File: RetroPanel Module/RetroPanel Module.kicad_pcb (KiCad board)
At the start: 2 copper layers, 100 x 97.9 mm, 77 parts, among them J1 Front Panel, J10 SW_EXTRA, J11 RS-232, J12 +5VSB, J13 PWR_ON, J14 PWR_OK, J15 COMMON, J16 SPEAKER, J17 LED_HDD, J2 SW_POWER, J3 LED_POWER, J4 SW_RESET, J5 SW_TURBO, J6 LED_TURBO, J7 POWER, J8 IIC, J9 POST_CARD, M1 Mounting_Pin, M10 Mounting_Pad, M11 Mounting_Pad, M12 Mounting_Pad, M13 Mounting_Pad, M14 Mounting_Pad, M15 Mounting_Pad, M16 Mounting_Pin, M2 Mounting_Pin, M3 Mounting_Pin, M4 Mounting_Pad, M5 Mounting_Pad, M6 Mounting_Pad, M7 Mounting_Pad, M8 Mounting_Pad, M9 Mounting_Pad, Q1 2N3904, Q2 2N3904, Q3 2N3904, Q4 2N3904, U1 MAX232, U2 NE555P

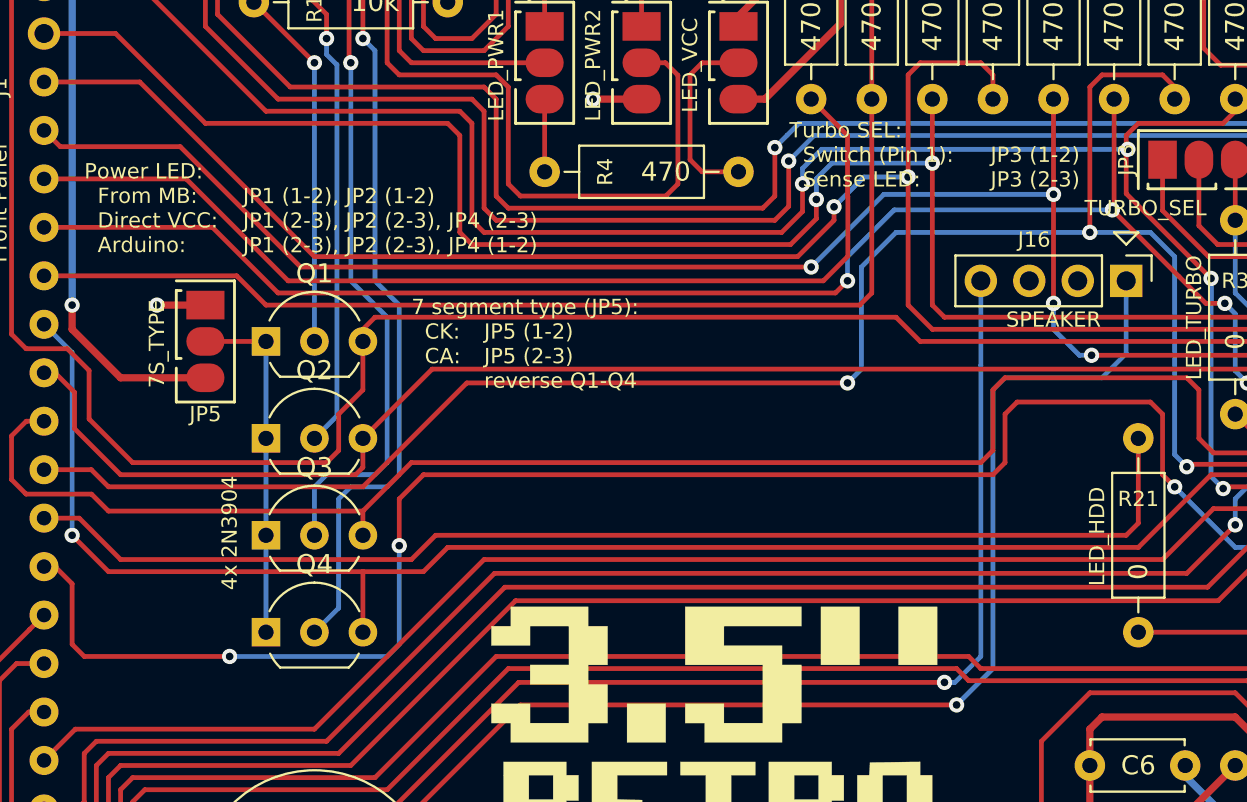
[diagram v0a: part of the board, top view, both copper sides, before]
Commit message: Better description for CA display usage
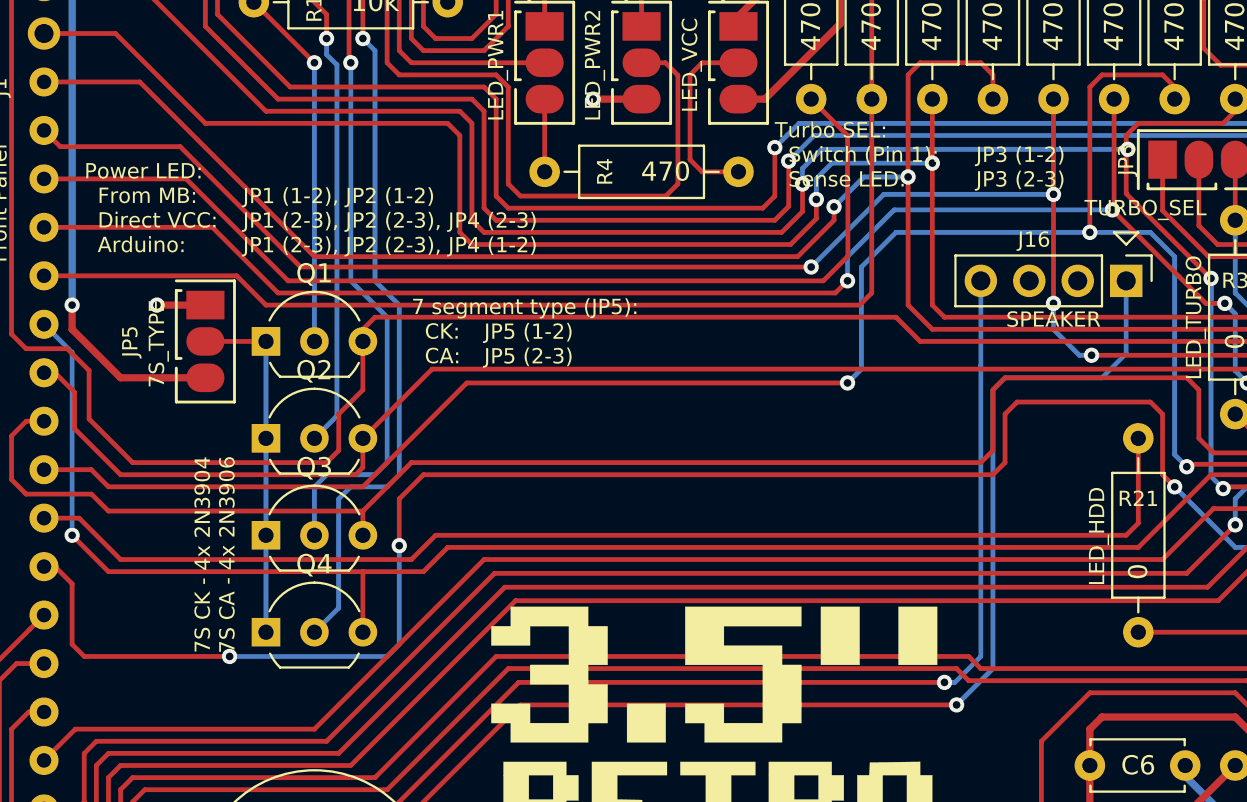
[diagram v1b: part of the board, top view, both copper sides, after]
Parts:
- Q1, Q2, Q3, Q4: value 2N3904 -> 2N3904/2N3906
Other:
- board text added: "7S CK - 4x 2N3904 7S CA - 4x 2N3906"
- board text added: "JP5 (1-2) JP5 (2-3)"
- board text removed: "4x 2N3904"
- board text removed: "JP5 (1-2) JP5 (2-3) reverse Q1-Q4"

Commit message: Tweaked resistor value to work better 7S CA
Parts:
- Q1, Q2, Q3, Q4: value 2N3904/2N3906 -> 2N3904 *
- R13, R14, R15, R16: value 10k -> 3k3
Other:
- board text added: "4x 2N3904 4x 2N3906 (install backwards)"
- board text added: "7 segment type (JP5): 7S CK: 7S CA:"
- board text added: "Q1-Q4: 7S CK: 7S CA:"
- board text removed: "7 segment type (JP5): CK: CA:"
- board text removed: "7S CK - 4x 2N3904 7S CA - 4x 2N3906"
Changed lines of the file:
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@@
   (general
     (thickness 1.6)
-    (drawings 86)
+    (drawings 87)
     (tracks 959)
     (zones 0)
@@
       (effects (font (size 0.8 0.8) (thickness 0.1)))
     )
-    (fp_text value 10k (at 3.81 0) (layer F.SilkS)
+    (fp_text value 3k3 (at 3.81 0) (layer F.SilkS)
       (effects (font (size 1 1) (thickness 0.15)))
     )
@@
       (effects (font (size 0.8 0.8) (thickness 0.1)))
     )
-    (fp_text value 10k (at 3.81 0) (layer F.SilkS)
+    (fp_text value 3k3 (at 3.81 0) (layer F.SilkS)
       (effects (font (size 1 1) (thickness 0.15)))
     )
@@
       (effects (font (size 0.8 0.8) (thickness 0.1)))
     )
-    (fp_text value 10k (at 3.81 0) (layer F.SilkS)
+    (fp_text value 3k3 (at 3.81 0) (layer F.SilkS)
       (effects (font (size 1 1) (thickness 0.15)))
     )
@@
       (effects (font (size 0.8 0.8) (thickness 0.1)))
     )
-    (fp_text value 10k (at 3.81 0) (layer F.SilkS)
+    (fp_text value 3k3 (at 3.81 0) (layer F.SilkS)
       (effects (font (size 1 1) (thickness 0.15)))
     )
@@
       (effects (font (size 1 1) (thickness 0.15)))
     )
-    (fp_text value 2N3904/2N3906 (at 2.54 2.79) (layer F.Fab)
+    (fp_text value "2N3904 *" (at 2.54 2.79) (layer F.Fab)
       (effects (font (size 1 1) (thickness 0.15)))
     )
@@
     (descr "TO-92 leads in-line, wide, drill 0.75mm (see NXP sot054_po.pdf)")
     (tags "to-92 sc-43 sc-43a sot54 PA33 transistor")
-    (fp_text reference Q2 (at 2.54 -3.56) (layer F.SilkS)
+    (fp_text reference Q2 (at -1.905 0 90) (layer F.SilkS)
       (effects (font (size 1 1) (thickness 0.15)))
     )
-    (fp_text value 2N3904/2N3906 (at 2.54 2.79) (layer F.Fab)
+    (fp_text value "2N3904 *" (at 2.54 2.79) (layer F.Fab)
       (effects (font (size 1 1) (thickness 0.15)))
     )
@@
     (descr "TO-92 leads in-line, wide, drill 0.75mm (see NXP sot054_po.pdf)")
     (tags "to-92 sc-43 sc-43a sot54 PA33 transistor")
-    (fp_text reference Q3 (at 2.54 -3.56) (layer F.SilkS)
+    (fp_text reference Q3 (at -1.905 0 90) (layer F.SilkS)
       (effects (font (size 1 1) (thickness 0.15)))
     )
-    (fp_text value 2N3904/2N3906 (at 2.54 2.79) (layer F.Fab)
+    (fp_text value "2N3904 *" (at 2.54 2.79) (layer F.Fab)
       (effects (font (size 1 1) (thickness 0.15)))
     )
@@
     (descr "TO-92 leads in-line, wide, drill 0.75mm (see NXP sot054_po.pdf)")
     (tags "to-92 sc-43 sc-43a sot54 PA33 transistor")
-    (fp_text reference Q4 (at 2.54 -3.56) (layer F.SilkS)
+    (fp_text reference Q4 (at -1.905 0 90) (layer F.SilkS)
       (effects (font (size 1 1) (thickness 0.15)))
     )
-    (fp_text value 2N3904/2N3906 (at 2.54 2.79) (layer F.Fab)
+    (fp_text value "2N3904 *" (at 2.54 2.79) (layer F.Fab)
       (effects (font (size 1 1) (thickness 0.15)))
     )
@@
     )
   )
+  (gr_text "\n4x 2N3904\n4x 2N3906 (install backwards)" (at 142.487 112.689) (layer F.SilkS)
+    (effects (font (size 0.8 0.8) (thickness 0.1)) (justify left))
+  )
   (gr_text LED_TURBO (at 177.666 110.276 90) (layer F.SilkS)
     (effects (font (size 0.8 0.8) (thickness 0.1)) (justify left))
@@
     (effects (font (size 0.8 0.8) (thickness 0.1)) (justify left))
   )
-  (gr_text "7S CK - 4x 2N3904\n7S CA - 4x 2N3906" (at 126.358 119.42 90) (layer F.SilkS)
-    (effects (font (size 0.8 0.8) (thickness 0.1)))
+  (gr_text "Q1-Q4:\n  7S CK:\n  7S CA:" (at 136.645 112.689) (layer F.SilkS)
+    (effects (font (size 0.8 0.8) (thickness 0.1)) (justify left))
   )
-  (gr_text "\nJP5 (1-2)\nJP5 (2-3)" (at 140.455 107.736) (layer F.SilkS)
+  (gr_text "\nJP5 (1-2)\nJP5 (2-3)" (at 142.487 107.736) (layer F.SilkS)
     (effects (font (size 0.8 0.8) (thickness 0.1)) (justify left))
   )
-  (gr_text "7 segment type (JP5):\n  CK:\n  CA:\n\n" (at 136.645 108.371) (layer F.SilkS)
+  (gr_text "7 segment type (JP5):\n  7S CK:\n  7S CA:\n\n" (at 136.645 108.371) (layer F.SilkS)
     (effects (font (size 0.8 0.8) (thickness 0.1)) (justify left))
   )

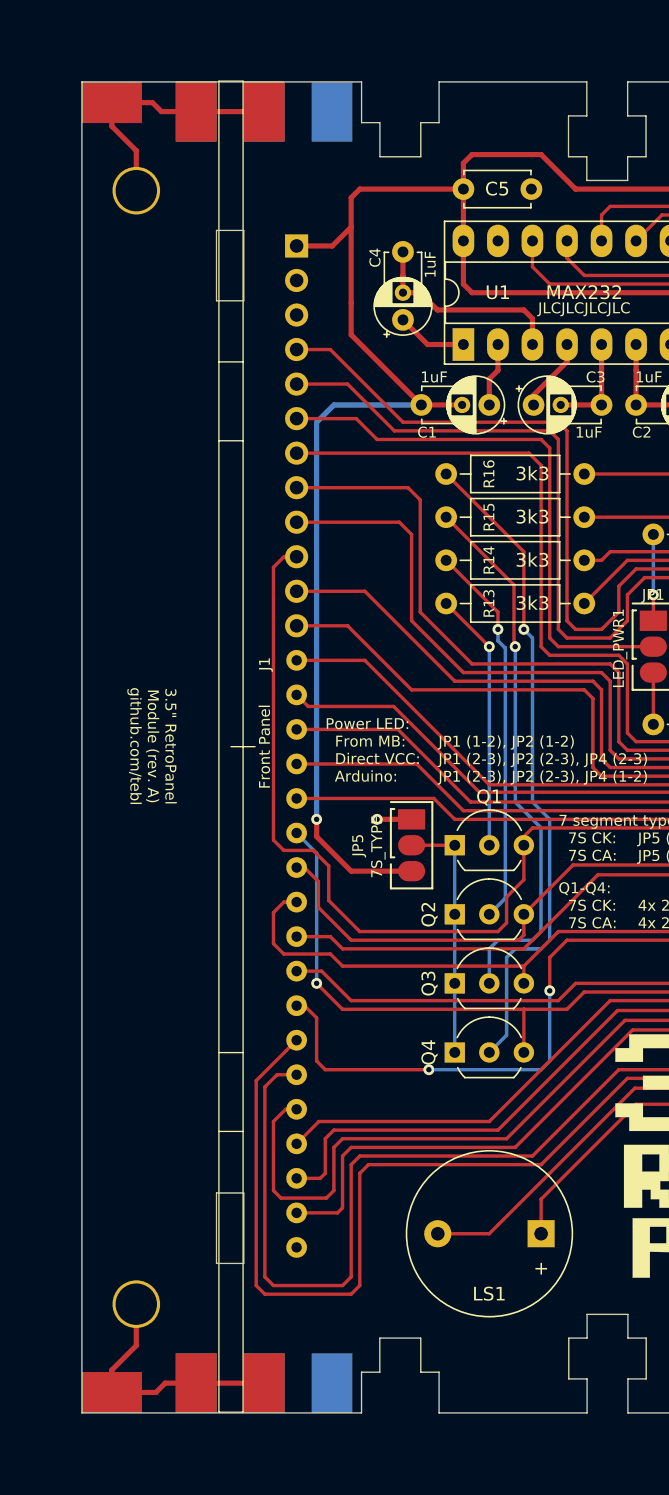
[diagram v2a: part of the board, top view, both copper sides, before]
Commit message: Adjustable mounting with huge pads
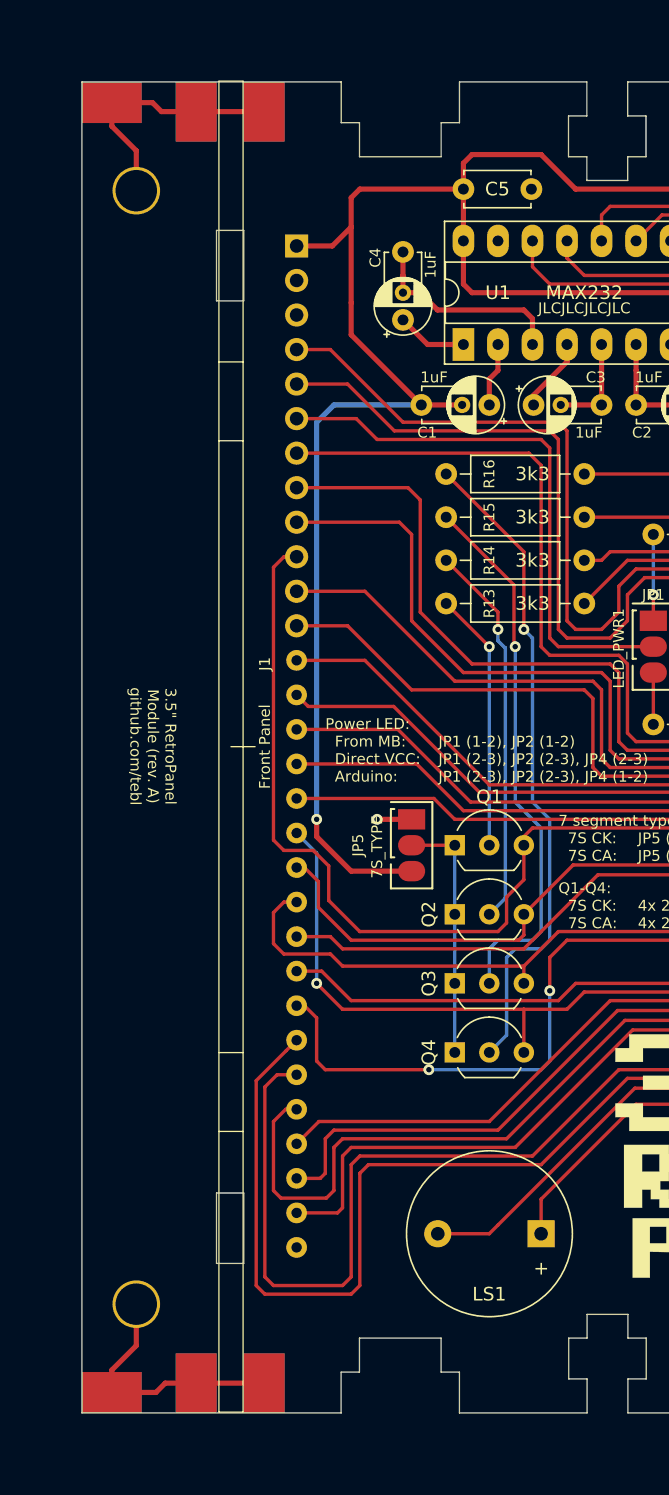
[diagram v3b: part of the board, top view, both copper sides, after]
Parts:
- removed M4, M6: Mounting_Pad, RetroPanel:B.Pad_pin
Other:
- outline, holes or cut-outs redrawn

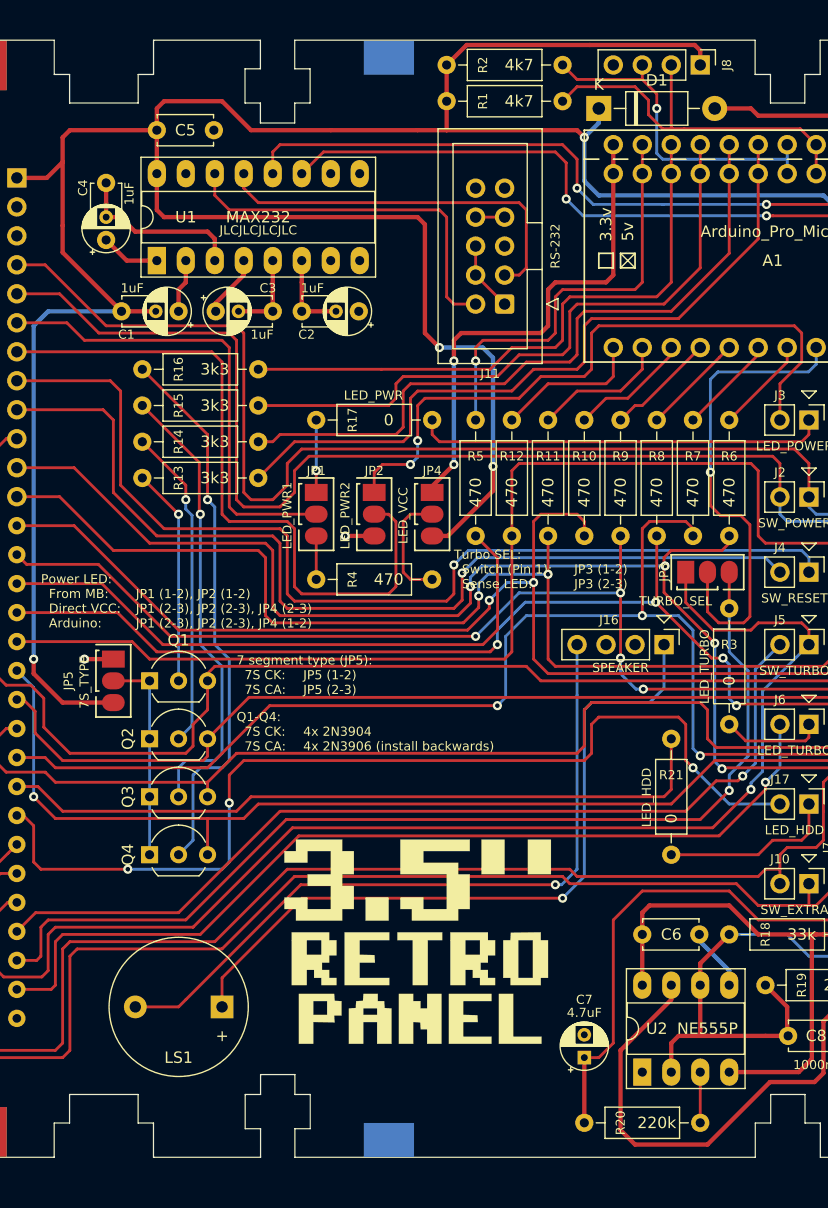
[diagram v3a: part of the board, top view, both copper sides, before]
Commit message: Optional standby power LED
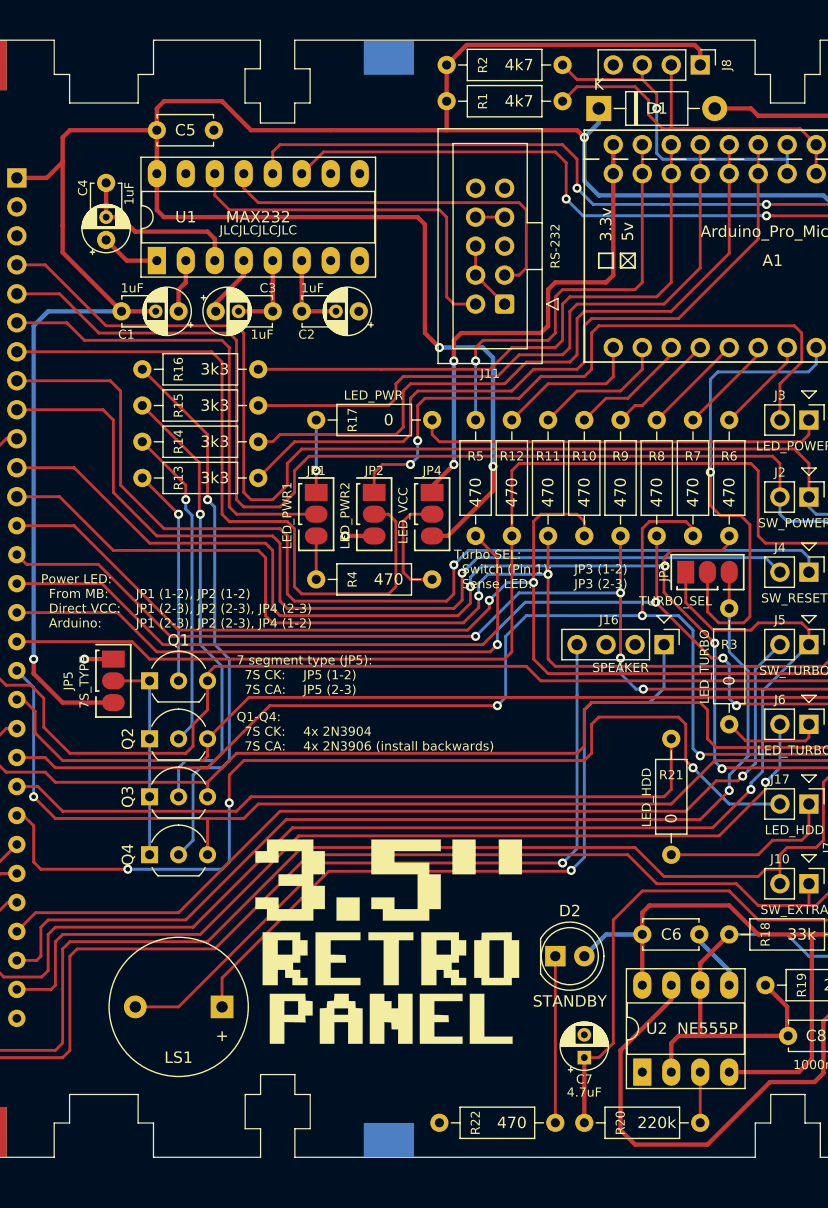
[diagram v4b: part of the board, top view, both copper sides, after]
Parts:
- added D2: STANDBY, LED_THT:LED_D5.0mm, F.Cu at (164.6, 132.4)
- added R22: 470, resistor:R_Axial_DIN0207_L6.3mm_D2.5mm_P10.16mm_Horizontal, F.Cu at (154.4, 147.0)
- moved G*** 2.54 mm to (150.0, 131.1)
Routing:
- net Net-(D2-Pad1): track 0.00 -> 14.6 mm
- net /Smart Switch/+5VSB: track 51.1 -> 56.9 mm
- net SW_EXTRA1: track 155.9 -> 157.5 mm
- net SW_EXTRA2: track 151.0 -> 152.6 mm
- net Net-(J16-Pad4): track 63.4 -> 62.3 mm
- net Net-(J16-Pad1): track 64.2 -> 63.2 mm

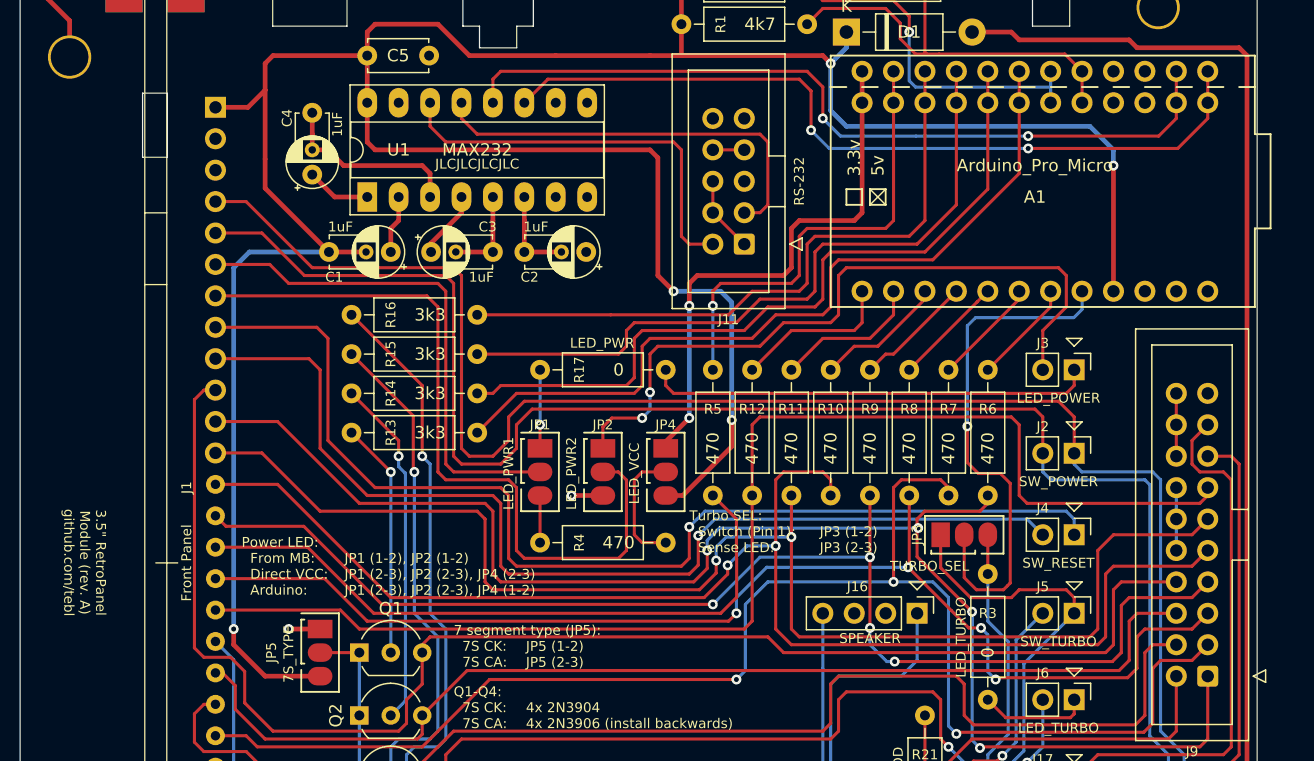
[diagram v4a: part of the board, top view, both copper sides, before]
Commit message: Fixed RS-232 connector and export files for second prototype
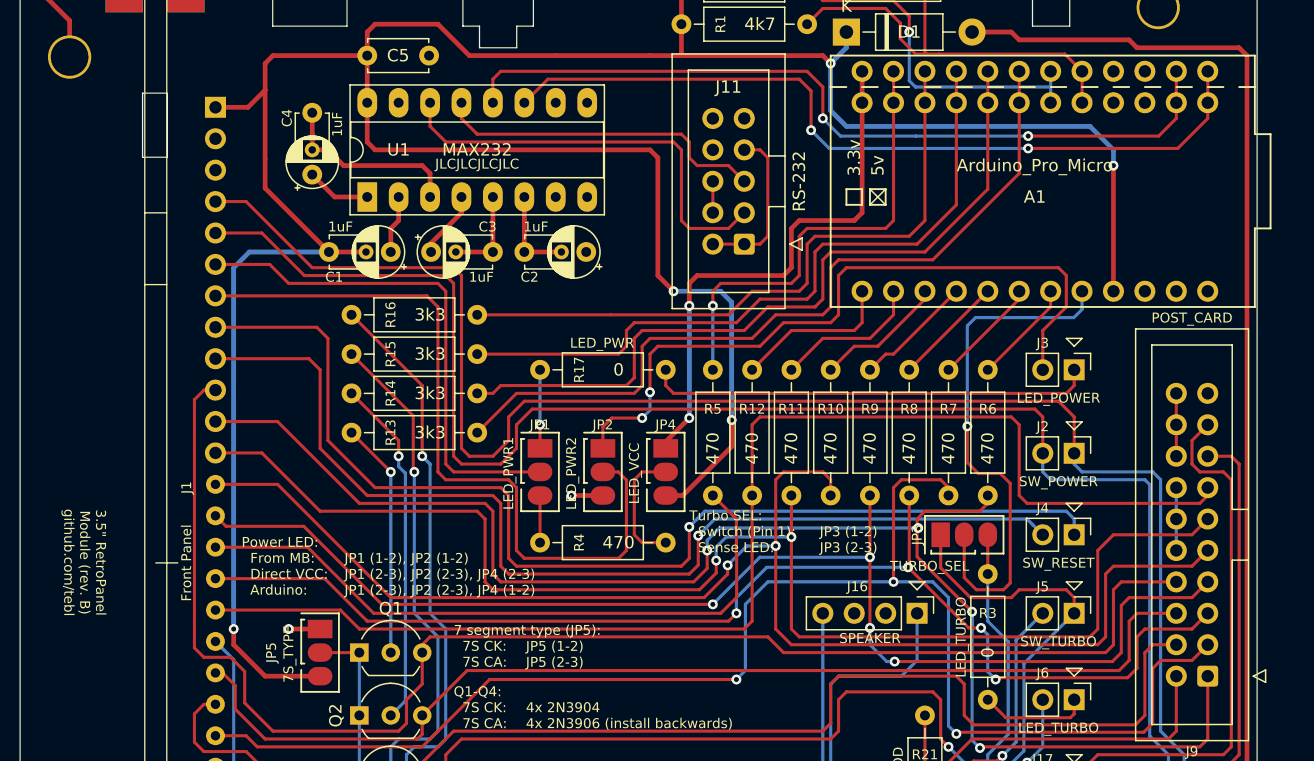
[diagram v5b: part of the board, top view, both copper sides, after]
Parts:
- J11: footprint Connector_IDC:IDC-Header_2x05_P2.54mm_Vertical -> RetroPanel:IDC-RS-232-Female
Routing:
- net Net-(J11-Pad1): track 6.13 -> 13.2 mm
- net RS232_RX: track 34.1 -> 27.0 mm
- net RS232_TX: track 32.8 -> 34.6 mm
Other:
- board text added: "3.5" RetroPanel Module (rev. B) github.com/tebl"
- board text removed: "3.5" RetroPanel Module (rev. A) github.com/tebl"
